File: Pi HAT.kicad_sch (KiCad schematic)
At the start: 11 parts, among them J1 Screw_Terminal_01x04, J4 Barrel_Jack, J5 Screw_Terminal_01x03, J6 Screw_Terminal_01x03, J7 GPIO_CONNECTOR, Q1 S8550

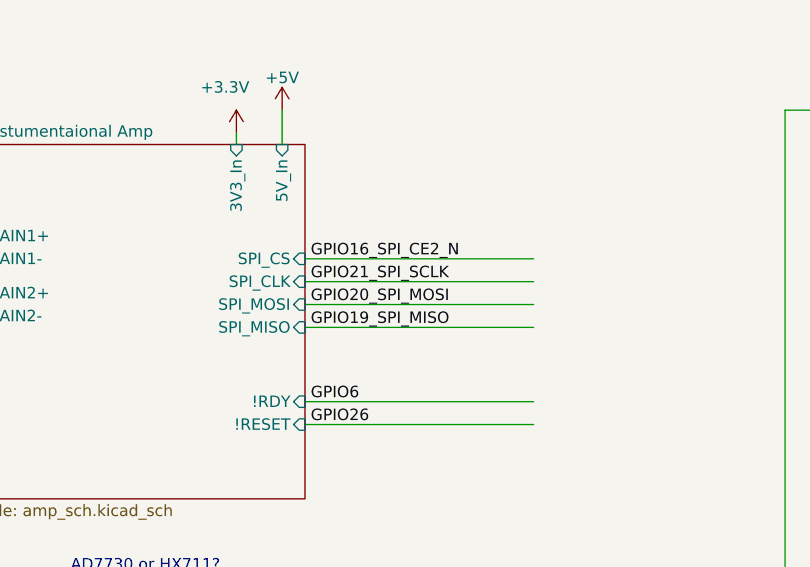
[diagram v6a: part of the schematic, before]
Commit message: Updated wiring. Test points only added for AD7730.
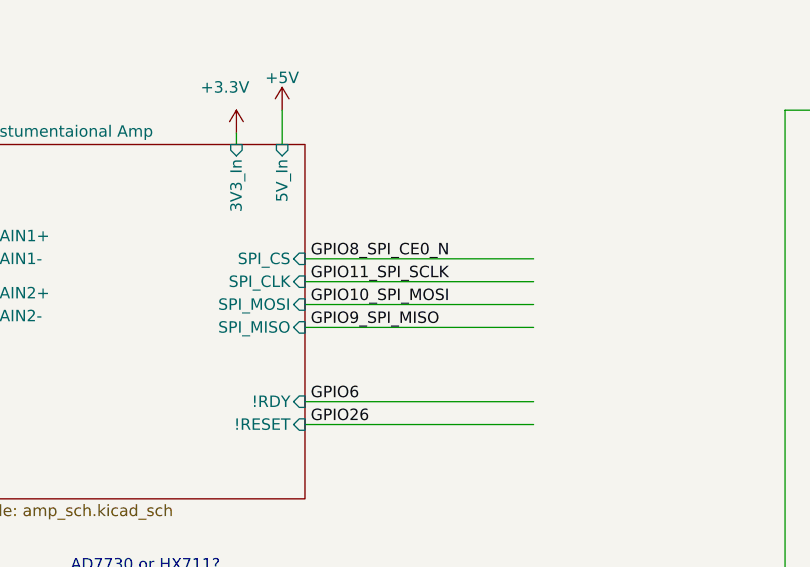
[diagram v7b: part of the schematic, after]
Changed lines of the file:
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@@
     (effects (font (size 1.27 1.27)) (justify left bottom))
   )
-  (label "GPIO19_SPI_MISO" (at 93.345 95.885 0)
+  (label "GPIO9_SPI_MISO" (at 93.345 95.885 0)
     (effects (font (size 1.27 1.27)) (justify left bottom))
   )
@@
     (effects (font (size 1.27 1.27)) (justify left bottom))
   )
-  (label "GPIO16_SPI_CE2_N" (at 93.345 88.265 0)
+  (label "GPIO8_SPI_CE0_N" (at 93.345 88.265 0)
     (effects (font (size 1.27 1.27)) (justify left bottom))
   )
@@
     (effects (font (size 1.27 1.27)) (justify left bottom))
   )
-  (label "GPIO20_SPI_MOSI" (at 93.345 93.345 0)
+  (label "GPIO10_SPI_MOSI" (at 93.345 93.345 0)
     (effects (font (size 1.27 1.27)) (justify left bottom))
   )
@@
     (effects (font (size 1.27 1.27)) (justify left bottom))
   )
-  (label "GPIO21_SPI_SCLK" (at 93.345 90.805 0)
+  (label "GPIO11_SPI_SCLK" (at 93.345 90.805 0)
     (effects (font (size 1.27 1.27)) (justify left bottom))
   )
@@
       (reference "R17") (unit 1) (value "1k") (footprint "Resistor_SMD:R_0402_1005Metric")
     )
-    (path "/715798e8-ada1-4b31-bdfe-4378c151d2b8/cca3808a-d6bb-44a3-ad1d-2a1c034fb726"
-      (reference "TP1") (unit 1) (value "TestPoint") (footprint "TestPoint:TestPoint_Pad_D1.5mm")
-    )
-    (path "/715798e8-ada1-4b31-bdfe-4378c151d2b8/73e3223a-0afd-438b-8fcb-933535615d47"
-      (reference "TP2") (unit 1) (value "TestPoint") (footprint "TestPoint:TestPoint_Pad_D1.5mm")
-    )
-    (path "/715798e8-ada1-4b31-bdfe-4378c151d2b8/6caf196e-dcfe-4294-9da5-689e6f22f042"
-      (reference "TP3") (unit 1) (value "TestPoint") (footprint "TestPoint:TestPoint_Pad_D1.5mm")
-    )
-    (path "/715798e8-ada1-4b31-bdfe-4378c151d2b8/3b600e6a-acbe-4f8c-ad56-d17f4e961218"
-      (reference "TP4") (unit 1) (value "TestPoint") (footprint "TestPoint:TestPoint_Pad_D1.5mm")
-    )
     (path "/5ec412a6-29a4-46a1-a19b-d00a58557335/e5da6f3f-d704-4afe-8d35-e0a9bac612ad"

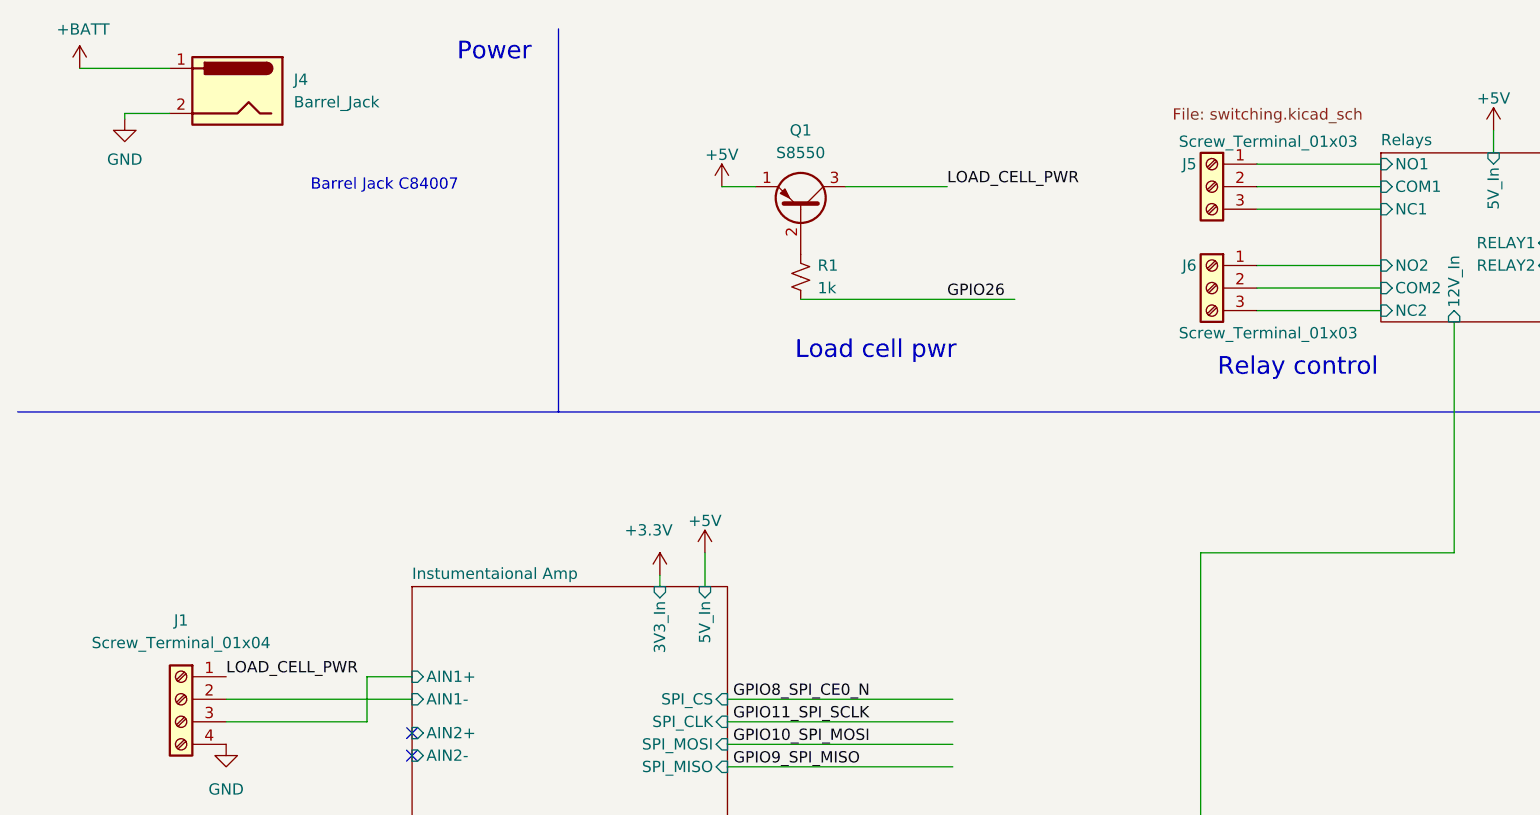
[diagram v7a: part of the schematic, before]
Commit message: Used Phoenix connectors. Wired ADC0 track.
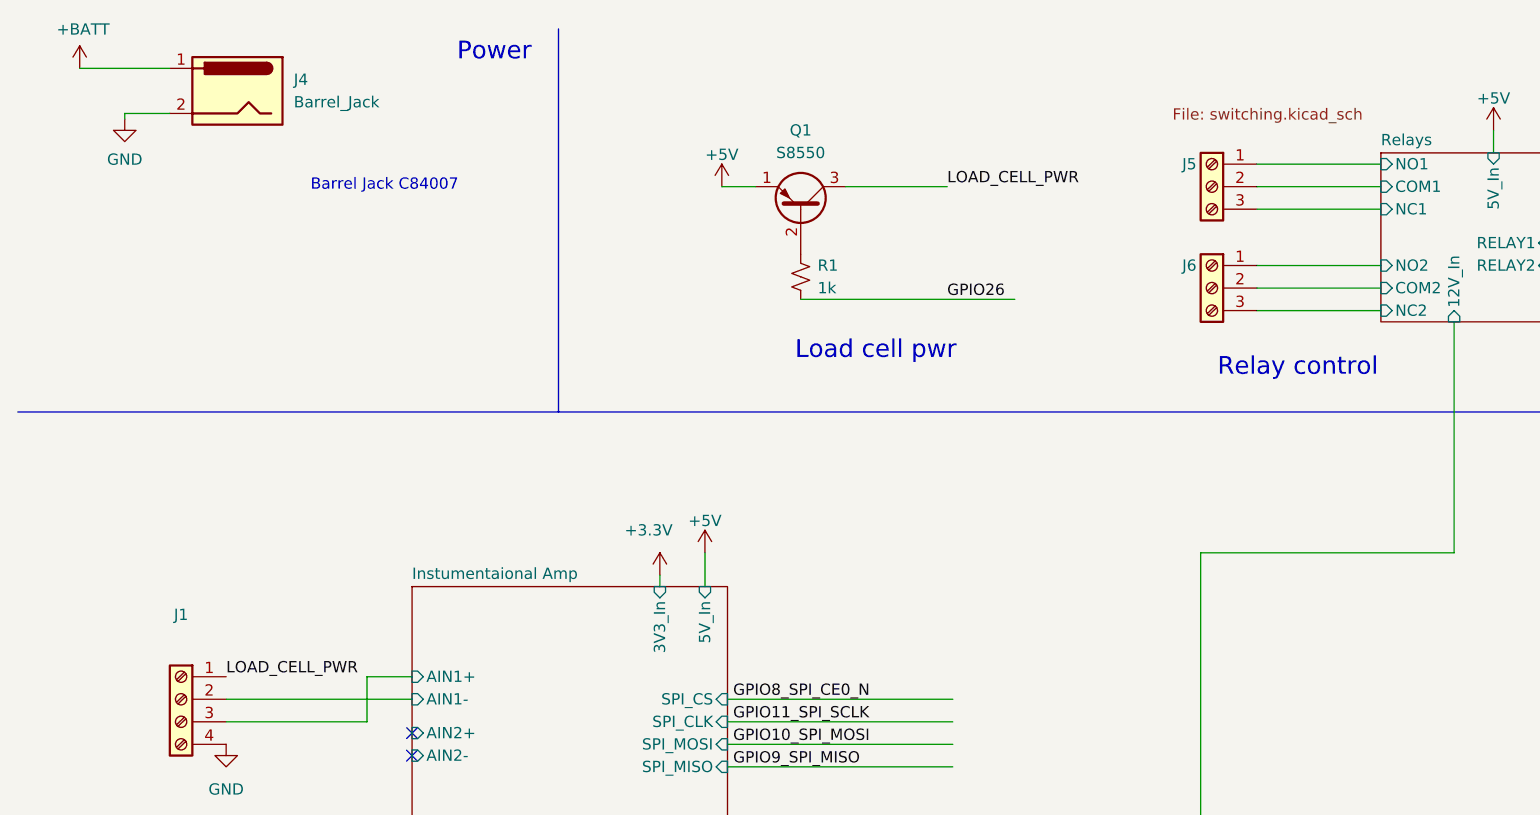
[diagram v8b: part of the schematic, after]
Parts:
- J1: value Screw_Terminal_01x04 -> (none); footprint TerminalBlock_4Ucon:TerminalBlock_4Ucon_1x04_P3.50mm_Vertical -> (none)
- J5, J6: value Screw_Terminal_01x03 -> (none); footprint TerminalBlock_4Ucon:TerminalBlock_4Ucon_1x03_P3.50mm_Vertical -> (none)
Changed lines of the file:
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@@
   (symbol (lib_id "Connector:Screw_Terminal_01x04") (at 31.115 88.265 0) (mirror y) (unit 1)
     (in_bom yes) (on_board yes) (fields_autoplaced)
-    (property "Reference" "J1" (id 0) (at 31.115 79.375 0))
-    (property "Value" "Screw_Terminal_01x04" (id 1) (at 31.115 81.915 0))
-    (property "Footprint" "TerminalBlock_4Ucon:TerminalBlock_4Ucon_1x04_P3.50mm_Vertical" (id 2) (at 31.115 88.265 0)
+    (property "Reference" "J1" (id 0) (at 31.115 78.74 0))
+    (property "Value" "" (id 1) (at 31.115 81.28 0))
+    (property "Footprint" "" (id 2) (at 31.115 88.265 0)
       (effects (font (size 1.27 1.27)) hide)
     )
@@
     (in_bom yes) (on_board yes)
     (property "Reference" "J5" (id 0) (at 144.78 27.94 0))
-    (property "Value" "Screw_Terminal_01x03" (id 1) (at 153.67 25.4 0))
-    (property "Footprint" "TerminalBlock_4Ucon:TerminalBlock_4Ucon_1x03_P3.50mm_Vertical" (id 2) (at 147.32 30.48 0)
+    (property "Value" "" (id 1) (at 153.67 25.4 0))
+    (property "Footprint" "" (id 2) (at 147.32 30.48 0)
       (effects (font (size 1.27 1.27)) hide)
     )
@@
     (in_bom yes) (on_board yes)
     (property "Reference" "J6" (id 0) (at 144.78 39.37 0))
-    (property "Value" "Screw_Terminal_01x03" (id 1) (at 153.67 46.99 0))
-    (property "Footprint" "TerminalBlock_4Ucon:TerminalBlock_4Ucon_1x03_P3.50mm_Vertical" (id 2) (at 147.32 41.91 0)
+    (property "Value" "" (id 1) (at 153.67 46.99 0))
+    (property "Footprint" "" (id 2) (at 147.32 41.91 0)
       (effects (font (size 1.27 1.27)) hide)
     )
@@
     )
     (path "/4971e12a-d07a-4b0a-8cfd-ea8bd16efa5a"
-      (reference "J1") (unit 1) (value "Screw_Terminal_01x04") (footprint "TerminalBlock_4Ucon:TerminalBlock_4Ucon_1x04_P3.50mm_Vertical")
+      (reference "J1") (unit 1) (value "Screw_Terminal_01x04") (footprint "TerminalBlock_Phoenix:TerminalBlock_Phoenix_PT-1,5-4-3.5-H_1x04_P3.50mm_Horizontal")
     )
     (path "/e7b3f30c-87be-4739-88d3-b191cd762eab"
@@
     )
     (path "/4d1584f9-1967-4133-999d-e82de878dab3"
-      (reference "J5") (unit 1) (value "Screw_Terminal_01x03") (footprint "TerminalBlock_4Ucon:TerminalBlock_4Ucon_1x03_P3.50mm_Vertical")
+      (reference "J5") (unit 1) (value "Screw_Terminal_01x03") (footprint "TerminalBlock_Phoenix:TerminalBlock_Phoenix_PT-1,5-3-3.5-H_1x03_P3.50mm_Horizontal")
     )
     (path "/e986c358-07b8-4241-b430-6ac1ca50103e"
-      (reference "J6") (unit 1) (value "Screw_Terminal_01x03") (footprint "TerminalBlock_4Ucon:TerminalBlock_4Ucon_1x03_P3.50mm_Vertical")
+      (reference "J6") (unit 1) (value "Screw_Terminal_01x03") (footprint "TerminalBlock_Phoenix:TerminalBlock_Phoenix_PT-1,5-3-3.5-H_1x03_P3.50mm_Horizontal")
     )
     (path "/00000000-0000-0000-0000-00005c77771f"
